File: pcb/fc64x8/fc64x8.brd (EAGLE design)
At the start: 20.3 x 31.8 mm, 42 parts, among them J1 Micro USB, J2 Outputs, U1 MK20DX128VLF5, U2 AAT3110IGU-5.0-T1, U3 SN74HCT245PWR, X1 16 MHz

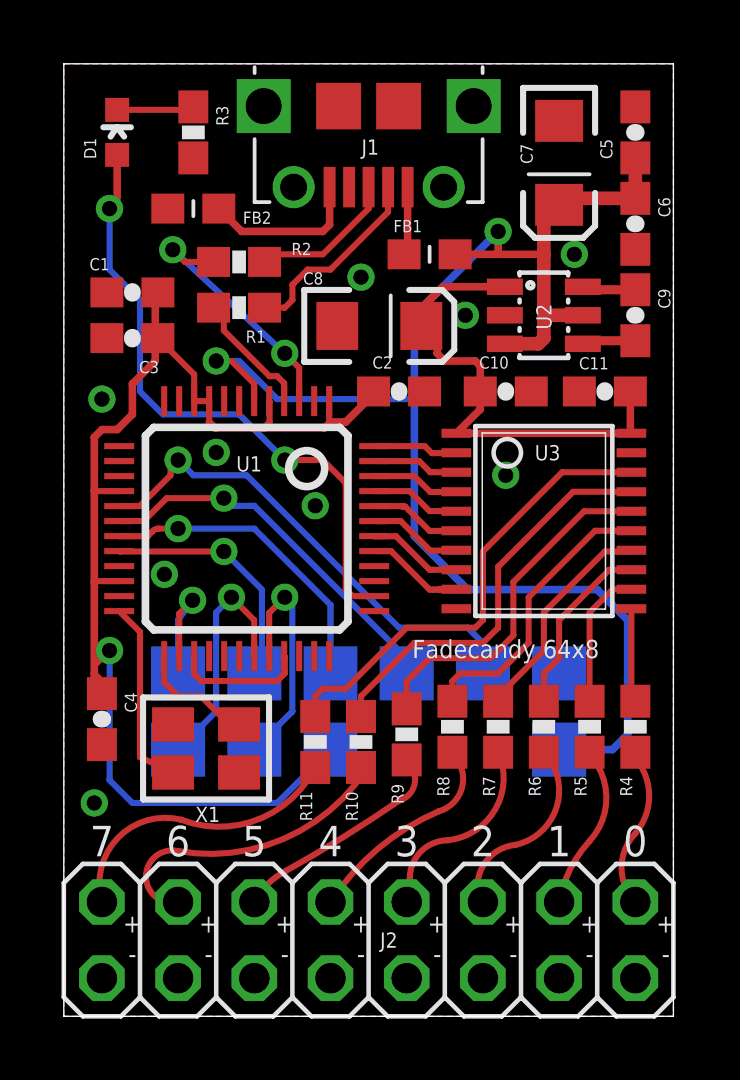
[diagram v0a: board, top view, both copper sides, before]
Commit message: Aesthetic adjustments and silkscreen width tweaks
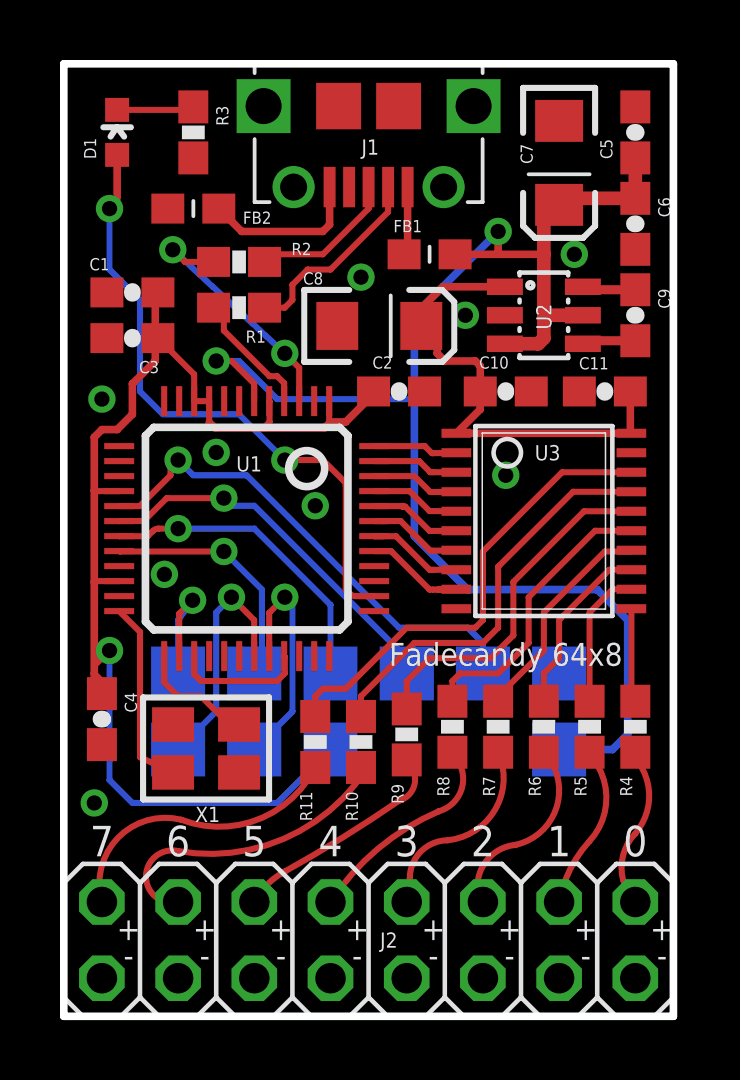
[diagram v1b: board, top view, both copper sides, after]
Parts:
- moved U$1 0.25 mm to (18.0, 29.5), turned to 0 degrees
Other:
- board text added: "MES '13"
- board text removed: "scanlime 2013"
